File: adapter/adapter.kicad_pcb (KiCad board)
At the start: 2 copper layers, 93.6 x 71.8 mm, 44 parts, among them J10 Ribbon, J11 Ribbon, J12 Ribbon, J13 serial, J14 serial, J3 battery charge, J6 battery charge, J7 trackball, J8 trackball, J9 Ribbon, SW1 SW_SPST, SW2 SW_SPST, SW3 SW_SPDT, SW4 SW_SPDT, U1 eliteC, U2 eliteC

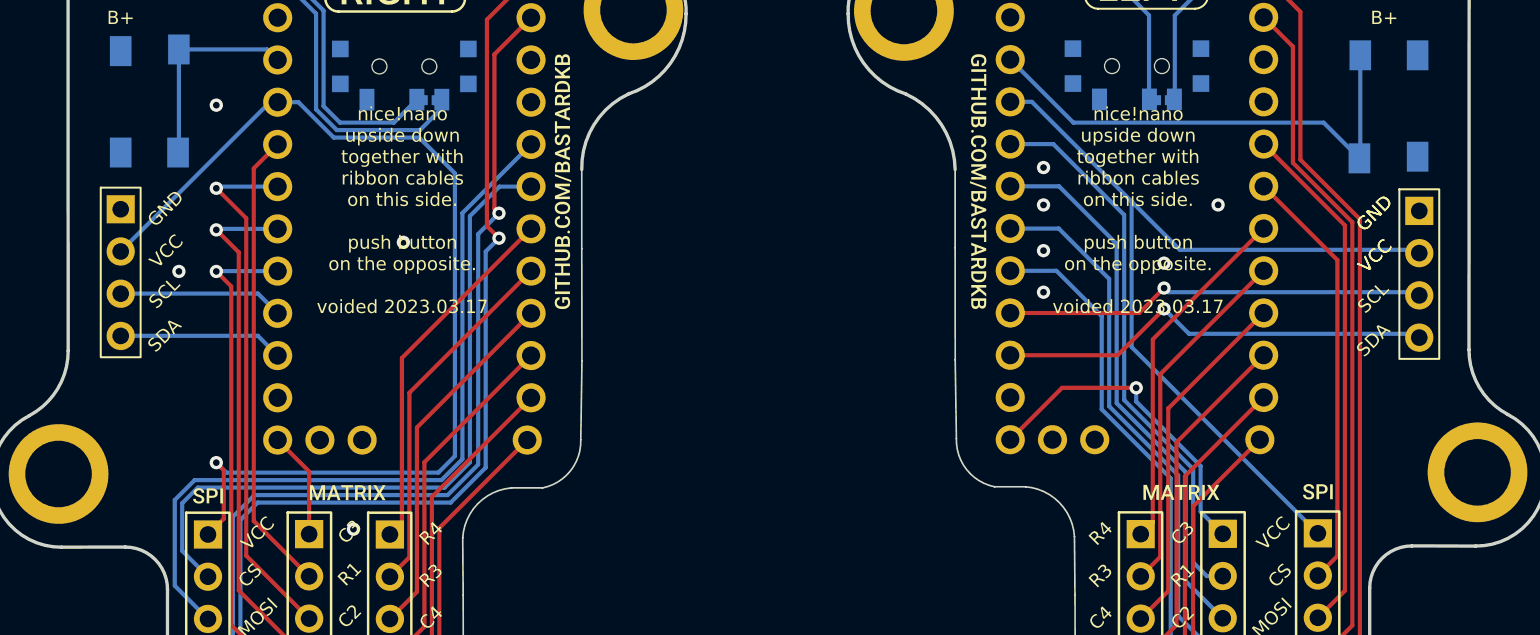
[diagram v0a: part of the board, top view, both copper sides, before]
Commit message: remove fill and unused serial connectors
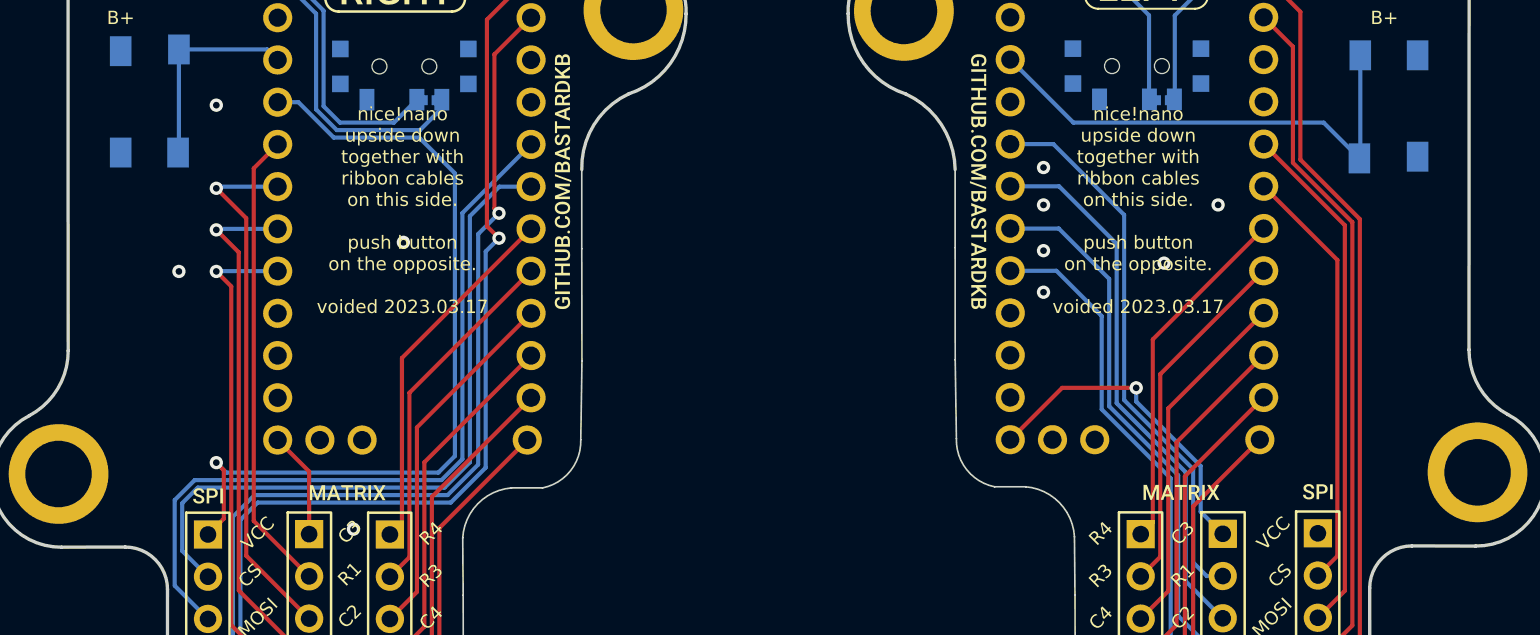
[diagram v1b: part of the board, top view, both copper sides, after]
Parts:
- removed J13, J14: serial, Library:PinHeader_1x04_P2.54mm_Vertical
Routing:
- net +5V: track 115.5 -> 49.3 mm
- net sda_r: track 26.5 -> 0.00 mm, vias 1 -> 0
- net scl_r: track 25.4 -> 0.00 mm, vias 1 -> 0
- net scl_l: track 9.94 -> 0.00 mm
- net sda_l: track 9.94 -> 0.00 mm
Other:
- board text removed: "SCL"
- board text removed: "SDA"

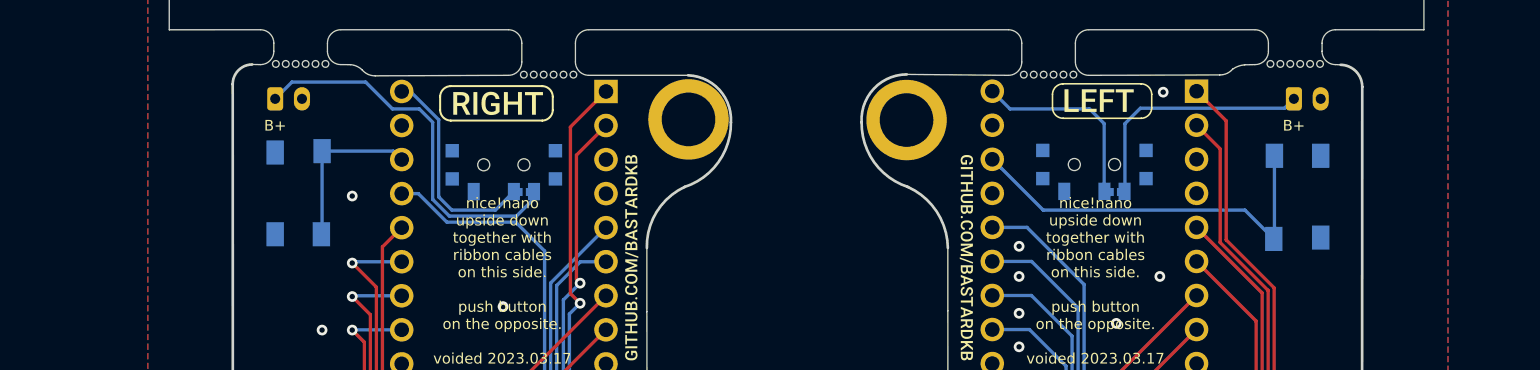
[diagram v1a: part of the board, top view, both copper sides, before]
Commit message: mark mousebites not in schematic
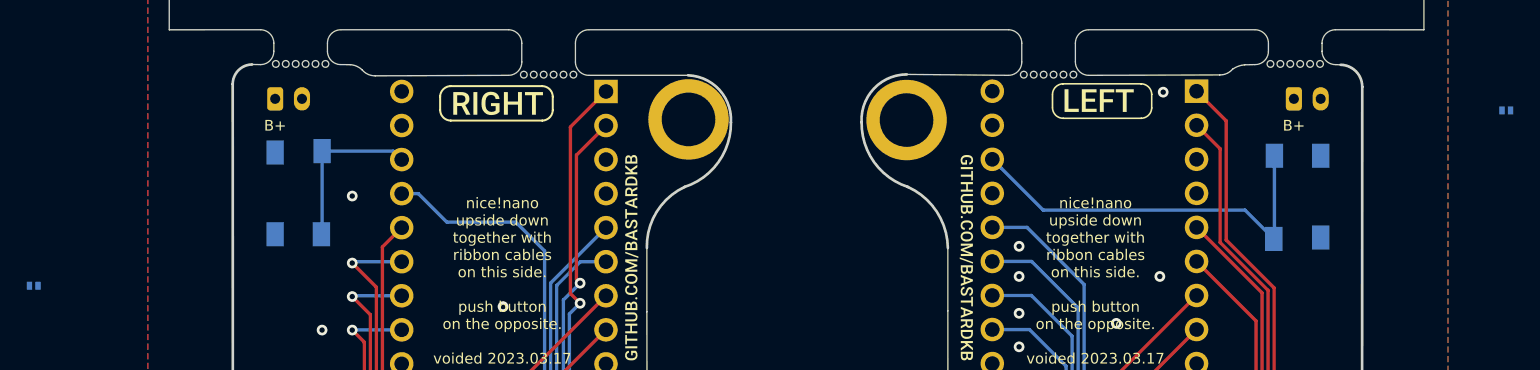
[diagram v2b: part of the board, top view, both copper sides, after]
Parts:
- removed SW3, SW4: SW_SPDT, Library:SW_SPDT+H-MSK12C01_hor(7pin_SMD)
- removed kibuzzard-620B8593 (x2): G***, kibuzzard-620B8593
- moved JP1 37.3 mm to (98.5, 83.7)
- moved JP2 29.8 mm to (208.3, 70.6)
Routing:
- net bat_sw_l: track 28.4 -> 0.00 mm
- net bat_sw_r: track 18.4 -> 0.00 mm
- net bat_l: track 16.0 -> 0.00 mm
- net bat_r: track 14.4 -> 0.00 mm

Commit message: simplify
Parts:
- removed JP1, JP2: Jumper_2_Open, Library:power_switch_jumper
- added SW3: SW_SPST, Library:200AWMSP2T2A1M6RE, F.Cu at (115.8, 76.7)
- added SW4: SW_SPST, Library:200AWMSP2T2A1M6RE, F.Cu at (190.2, 76.6)
- SW1, SW2: moved to F.Cu
- moved J3 22.7 mm to (116.5, 92.4), turned to 90 degrees
- moved J6 20.8 mm to (194.8, 90.4), turned to -90 degrees
- moved SW1 6.51 mm to (116.6, 83.1)
- moved SW2 6.15 mm to (194.3, 83.1)
- moved REF** 0.13 mm to (118.5, 67.2)
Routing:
- net bat_sw_l: track 0.00 -> 17.6 mm, vias 0 -> 1
- net Rst: track 12.4 -> 23.4 mm
- net bat_l: track 0.00 -> 10.7 mm
- net Rst2: track 29.7 -> 37.3 mm, vias 0 -> 1
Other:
- board text added: "nice!nano upside down together with ribbon cables on this side."
- board text removed: "nice!nano upside down together with ribbon cables on this side. push button on the opposite. voided 2023.03.17"

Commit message: tailor
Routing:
- net +5V: track 49.3 -> 83.5 mm
- net bat_r: track 0.00 -> 25.9 mm
- net bat_sw_r: track 0.00 -> 14.4 mm, vias 0 -> 1
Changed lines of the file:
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@@
   (gr_line (start 134.36262 63.83766) (end 134.36262 62.39766)
     (stroke (width 0.05) (type solid)) (layer "B.CrtYd"))
-  (gr_rect (start 111.79 98.452403) (end 129.54 112.452403)
-    (stroke (width 0.05) (type solid)) (fill none) (layer "B.CrtYd"))
   (gr_line (start 121.356968 63.797775) (end 121.356968 62.357775)
     (stroke (width 0.05) (type solid)) (layer "B.CrtYd"))
@@
   (via (at 182.75 69.25) (size 0.8) (drill 0.4) (layers "F.Cu" "B.Cu") (free) (net 27))
   (via (at 172 83) (size 0.8) (drill 0.4) (layers "F.Cu" "B.Cu") (free) (net 27))
-  (via (at 122.25 77) (size 0.8) (drill 0.4) (layers "F.Cu" "B.Cu") (free) (net 27))
+  (via (at 122.936 76.581) (size 0.8) (drill 0.4) (layers "F.Cu" "B.Cu") (free) (net 27))
   (segment (start 122.7 98.95) (end 122.7 101.869999) (width 0.25) (layer "F.Cu") (net 32))
   (segment (start 122.7 101.869999) (end 121.75 102.819999) (width 0.25) (layer "F.Cu") (net 32))
@@
   (segment (start 122.25 98.5) (end 122.85 99.1) (width 0.25) (layer "B.Cu") (net 32))
   (segment (start 134.45 78.95) (end 129.313604 78.95) (width 0.25) (layer "B.Cu") (net 32))
+  (segment (start 182.118 88.076895) (end 170.841105 76.8) (width 0.25) (layer "B.Cu") (net 32))
+  (segment (start 170.841105 76.8) (end 170 76.8) (width 0.25) (layer "B.Cu") (net 32))
   (segment (start 136.6 98.104416) (end 136.6 81.1) (width 0.25) (layer "B.Cu") (net 32))
+  (segment (start 188.5 102.75) (end 182.118 96.368) (width 0.25) (layer "B.Cu") (net 32))
+  (segment (start 182.118 96.368) (end 182.118 88.076895) (width 0.25) (layer "B.Cu") (net 32))
   (segment (start 136.6 81.1) (end 134.45 78.95) (width 0.25) (layer "B.Cu") (net 32))
   (segment (start 129.313604 78.95) (end 127.183604 76.82) (width 0.25) (layer "B.Cu") (net 32))
@@
   (segment (start 118.4828 76.6572) (end 118.3132 76.6572) (width 0.25) (layer "F.Cu") (net 39))
   (segment (start 125.94 69.2) (end 118.4828 76.6572) (width 0.25) (layer "F.Cu") (net 39))
+  (segment (start 189.2383 73.0587) (end 192.786 76.6064) (width 0.25) (layer "B.Cu") (net 40))
+  (segment (start 170 69.18) (end 173.8787 73.0587) (width 0.25) (layer "B.Cu") (net 40))
+  (segment (start 173.8787 73.0587) (end 189.2383 73.0587) (width 0.25) (layer "B.Cu") (net 40))
   (segment (start 116.544002 92.439998) (end 120.904 88.08) (width 0.25) (layer "F.Cu") (net 41))
   (segment (start 120.904 88.08) (end 120.904 81.788) (width 0.25) (layer "F.Cu") (net 41))
@@
   (segment (start 120.8532 81.7372) (end 120.8532 76.6572) (width 0.25) (layer "B.Cu") (net 41))
   (segment (start 120.904 81.788) (end 120.8532 81.7372) (width 0.25) (layer "B.Cu") (net 41))
+  (segment (start 194.31 77.6224) (end 194.31 82.296) (width 0.25) (layer "F.Cu") (net 42))
+  (segment (start 195.326 76.6064) (end 194.31 77.6224) (width 0.25) (layer "F.Cu") (net 42))
+  (via (at 194.31 82.296) (size 0.8) (drill 0.4) (layers "F.Cu" "B.Cu") (net 42))
+  (segment (start 194.31 82.296) (end 194.31 89.948) (width 0.25) (layer "B.Cu") (net 42))
+  (segment (start 194.31 89.948) (end 194.786 90.424) (width 0.25) (layer "B.Cu") (net 42))
   (zone (net 27) (net_name "GND") (layers "F&B.Cu") (hatch edge 0.5)
     (connect_pads (clearance 0.508))
     (min_thickness 0.25) (filled_areas_thickness no)
-    (fill (thermal_gap 0.5) (thermal_bridge_width 0.5))
+    (fill yes (thermal_gap 0.5) (thermal_bridge_width 0.5))
     (polygon
       (pts

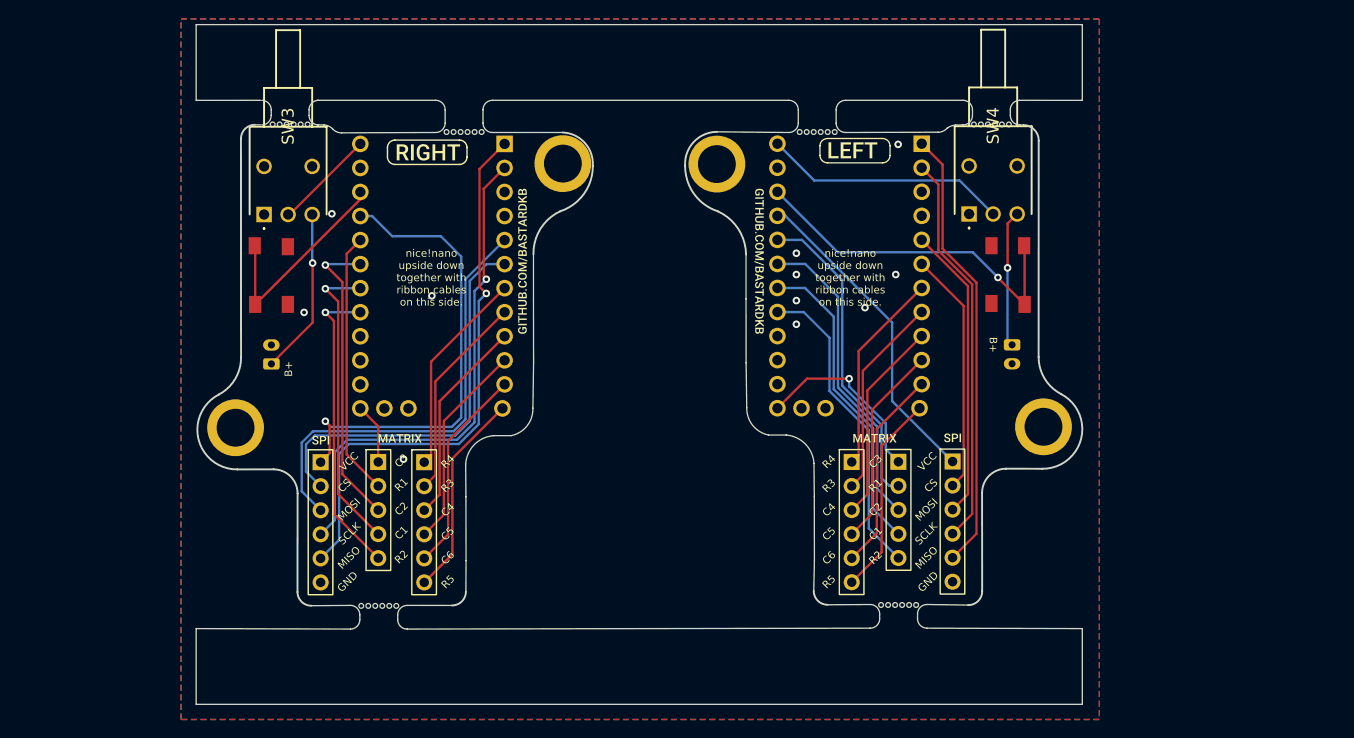
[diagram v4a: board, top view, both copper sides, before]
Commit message: update keeping holes
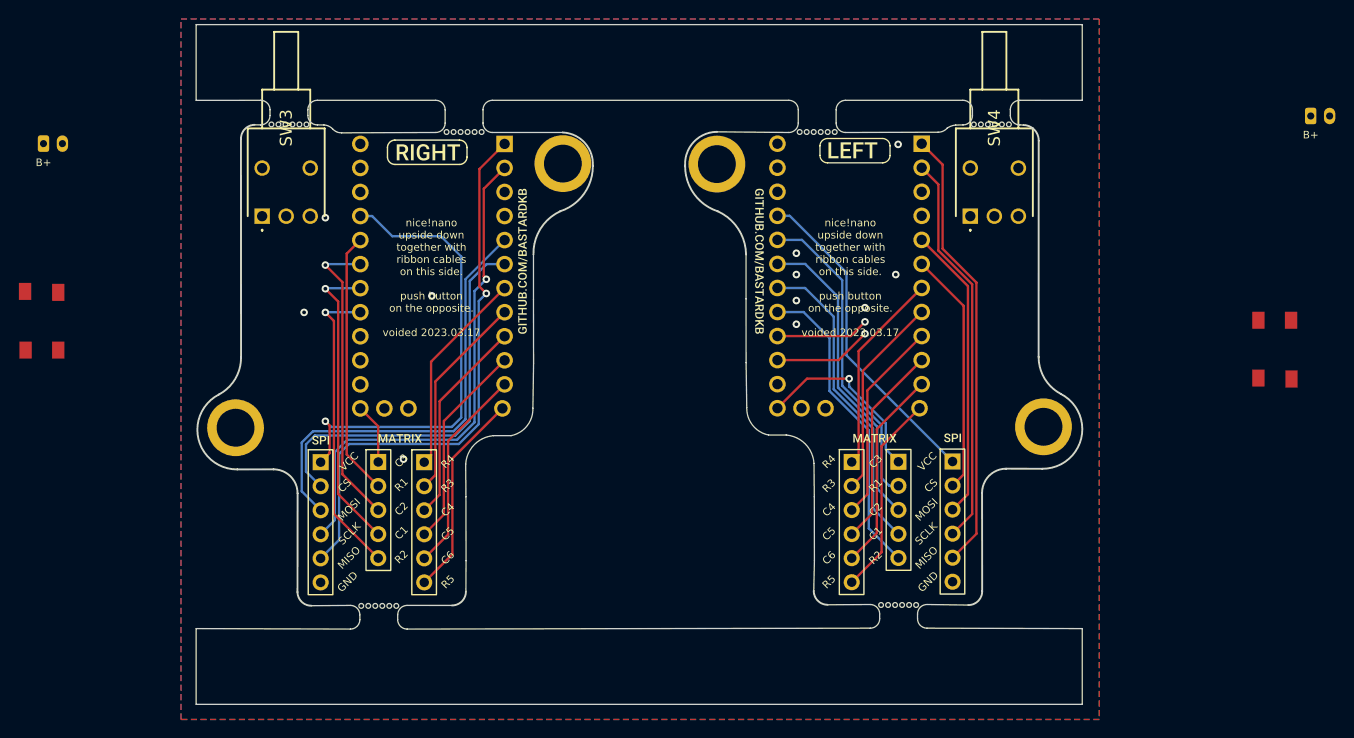
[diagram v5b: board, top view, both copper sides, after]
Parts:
- moved J6 39.7 mm to (226.3, 66.3), turned to 0 degrees
- moved J3 33.5 mm to (92.5, 69.2), turned to 0 degrees
- moved SW2 29.3 mm to (222.5, 90.9)
- moved SW1 24.7 mm to (92.3, 87.9)
- moved SW3 0.27 mm to (115.6, 76.8)
- moved SW4 0.26 mm to (190.4, 76.8)
- moved REF** 0.13 mm to (118.4, 67.2)
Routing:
- net Rst2: track 37.3 -> 0.00 mm, vias 1 -> 0
- net bat_r: track 25.9 -> 0.00 mm
- net Rst: track 23.4 -> 0.00 mm
- net bat_sw_l: track 17.6 -> 0.00 mm, vias 1 -> 0
- net bat_sw_r: track 14.4 -> 0.00 mm, vias 1 -> 0
- net bat_l: track 10.7 -> 0.00 mm
- net sda_r: track 0.00 -> 10.4 mm, vias 0 -> 1
- net scl_r: track 0.00 -> 9.87 mm, vias 0 -> 1
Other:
- board text added: "nice!nano upside down together with ribbon cables on this side. push button on the opposite. voided 2023.03.17"
- board text removed: "nice!nano upside down together with ribbon cables on this side."

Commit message: place
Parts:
- moved J6 41.8 mm to (193.3, 91.9)
- moved J3 32.5 mm to (116.2, 91.3)
- moved SW2 29.2 mm to (194.3, 83.3)
- moved SW1 24.8 mm to (116.7, 83.3)
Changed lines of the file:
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@@
   )
   (footprint "Connector_JST:JST_PH_B2B-PH-K_1x02_P2.00mm_Vertical" (layer "F.Cu")
-    (at 226.33 66.252)
+    (at 193.294 91.853)
     (descr "JST PH series connector, B2B-PH-K (http://www.jst-mfg.com/product/pdf/eng/ePH.pdf), generated with kicad-footprint-generator")
     (tags "connector JST PH side entry")
@@
   )
   (footprint "Library:PushSwitch" (layer "F.Cu")
-    (at 222.504 90.932 -90)
+    (at 194.31 83.312 -90)
     (descr "tactile push button, 6x6mm e.g. PTS645xx series, height=9.5mm")
     (tags "tact sw push 6mm smd")
@@
   )
   (footprint "Library:PushSwitch" (layer "F.Cu")
-    (at 92.329 87.884 90)
+    (at 116.713 83.312 90)
     (descr "tactile push button, 6x6mm e.g. PTS645xx series, height=9.5mm")
     (tags "tact sw push 6mm smd")
@@
   )
   (footprint "Connector_JST:JST_PH_B2B-PH-K_1x02_P2.00mm_Vertical" (layer "F.Cu")
-    (at 92.472 69.173)
+    (at 116.205 91.345)
     (descr "JST PH series connector, B2B-PH-K (http://www.jst-mfg.com/product/pdf/eng/ePH.pdf), generated with kicad-footprint-generator")
     (tags "connector JST PH side entry")
@@
     (effects (font (size 0.8 0.8) (thickness 0.15)) (justify mirror))
   )
-  (gr_text "B+" (at 225.806 67.945) (layer "B.SilkS")
+  (gr_text "B+" (at 192.77 93.546) (layer "B.SilkS")
     (effects (font (size 0.8 0.8) (thickness 0.15)) (justify mirror))
   )
@@
     (effects (font (size 0.8 0.8) (thickness 0.15)) (justify mirror))
   )
-  (gr_text "B+" (at 92.075 70.993) (layer "B.SilkS")
+  (gr_text "B+" (at 115.808 93.165) (layer "B.SilkS")
     (effects (font (size 0.8 0.8) (thickness 0.15)) (justify mirror))
   )
@@
     (effects (font (size 0.8 0.8) (thickness 0.15)))
   )
-  (gr_text "B+" (at 92.472 71.173) (layer "F.SilkS")
+  (gr_text "B+" (at 116.205 93.345) (layer "F.SilkS")
     (effects (font (size 0.8 0.8) (thickness 0.15)))
   )
@@
     (effects (font (size 0.8 0.8) (thickness 0.15)))
   )
-  (gr_text "B+" (at 226.33 68.252) (layer "F.SilkS")
+  (gr_text "B+" (at 193.294 93.853) (layer "F.SilkS")
     (effects (font (size 0.8 0.8) (thickness 0.15)))
   )

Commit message: route
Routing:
- net Rst2: track 0.00 -> 37.4 mm, vias 0 -> 1
- net bat_r: track 0.00 -> 26.1 mm
- net Rst: track 0.00 -> 23.0 mm
- net bat_sw_l: track 0.00 -> 16.4 mm
- net bat_sw_r: track 0.00 -> 15.9 mm
- net bat_l: track 0.00 -> 11.0 mm
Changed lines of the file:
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@@
   (gr_line (start 134.36262 63.83766) (end 134.36262 62.39766)
     (stroke (width 0.05) (type solid)) (layer "B.CrtYd"))
-  (gr_rect (start 111.79 98.452403) (end 129.54 112.452403)
-    (stroke (width 0.05) (type solid)) (fill none) (layer "B.CrtYd"))
   (gr_line (start 121.356968 63.797775) (end 121.356968 62.357775)
     (stroke (width 0.05) (type solid)) (layer "B.CrtYd"))
@@
     (effects (font (size 0.8 0.8) (thickness 0.15)))
   )
+  (segment (start 114.913 80.212) (end 114.913 80.242) (width 0.25) (layer "F.Cu") (net 1))
+  (segment (start 114.963 80.49) (end 114.963 86.412) (width 0.25) (layer "F.Cu") (net 1))
+  (segment (start 114.913 80.242) (end 115.062 80.391) (width 0.25) (layer "F.Cu") (net 1))
+  (segment (start 114.963 85.951) (end 114.963 86.412) (width 0.25) (layer "F.Cu") (net 1))
+  (segment (start 125.94 74.974) (end 114.963 85.951) (width 0.25) (layer "F.Cu") (net 1))
+  (segment (start 125.94 74.28) (end 125.94 74.974) (width 0.25) (layer "F.Cu") (net 1))
+  (segment (start 115.062 80.391) (end 114.963 80.49) (width 0.25) (layer "F.Cu") (net 1))
+  (segment (start 196.06 80.212) (end 196.06 86.362) (width 0.25) (layer "F.Cu") (net 2))
+  (segment (start 196.013 86.412) (end 196.11 86.412) (width 0.25) (layer "F.Cu") (net 2))
+  (segment (start 196.06 86.362) (end 196.11 86.412) (width 0.25) (layer "F.Cu") (net 2))
+  (segment (start 190.119 80.518) (end 196.013 86.412) (width 0.25) (layer "F.Cu") (net 2))
+  (via (at 190.119 80.518) (size 0.8) (drill 0.4) (layers "F.Cu" "B.Cu") (net 2))
+  (segment (start 190.0957 80.5413) (end 190.119 80.518) (width 0.25) (layer "B.Cu") (net 2))
+  (segment (start 170 74.26) (end 176.2813 80.5413) (width 0.25) (layer "B.Cu") (net 2))
+  (segment (start 176.2813 80.5413) (end 190.0957 80.5413) (width 0.25) (layer "B.Cu") (net 2))
   (segment (start 139.276396 81.9) (end 137.5 83.676396) (width 0.25) (layer "B.Cu") (net 3))
   (segment (start 120.2 103.809999) (end 121.75 105.359999) (width 0.25) (layer "B.Cu") (net 3))
@@
   (segment (start 190.125 84.225) (end 185.24 79.34) (width 0.25) (layer "F.Cu") (net 38))
   (segment (start 188.5 107.83) (end 190.125 106.205) (width 0.25) (layer "F.Cu") (net 38))
+  (segment (start 125.94 69.2) (end 118.305 76.835) (width 0.25) (layer "B.Cu") (net 39))
+  (segment (start 118.305 76.835) (end 118.11 76.835) (width 0.25) (layer "B.Cu") (net 39))
+  (segment (start 191.643 75.565) (end 192.913 76.835) (width 0.25) (layer "B.Cu") (net 40))
+  (segment (start 170 69.18) (end 176.385 75.565) (width 0.25) (layer "B.Cu") (net 40))
+  (segment (start 176.385 75.565) (end 191.643 75.565) (width 0.25) (layer "B.Cu") (net 40))
+  (segment (start 120.65 76.835) (end 116.205 81.28) (width 0.25) (layer "B.Cu") (net 41))
+  (segment (start 116.205 81.28) (end 116.205 91.345) (width 0.25) (layer "B.Cu") (net 41))
+  (segment (start 193.294 78.994) (end 195.453 76.835) (width 0.25) (layer "B.Cu") (net 42))
+  (segment (start 193.294 91.853) (end 193.294 78.994) (width 0.25) (layer "B.Cu") (net 42))
   (zone (net 27) (net_name "GND") (layers "F&B.Cu") (hatch edge 0.5)
     (connect_pads (clearance 0.508))
     (min_thickness 0.25) (filled_areas_thickness no)
-    (fill (thermal_gap 0.5) (thermal_bridge_width 0.5))
+    (fill yes (thermal_gap 0.5) (thermal_bridge_width 0.5))
     (polygon
       (pts
